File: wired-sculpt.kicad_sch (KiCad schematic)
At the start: 39 parts, among them J1 10103594-0001LF, J2 FFC3B07-30-T, J3 AVR-ISP-6 - NOT FITTED, Q1 BSS84AK,215, Q2 2N7002BK,215, SW1 FSMSM, SW2 S2B-PH-K-S(LF)(SN), U1 USBLC6-2SC6, U2 LM2776DBVT, U3 AT90USB1286-AUR, Y1 TSX-3225 16.0000MF18X-AC0

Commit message: Exclude holes and ISP from BOM
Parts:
- H1, H2, H3, J3: now left out of the parts list
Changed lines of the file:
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@@
   )
   (symbol (lib_id "Connector:AVR-ISP-6") (at 210.82 36.83 0) (mirror y) (unit 1)
-    (in_bom yes) (on_board yes)
+    (in_bom no) (on_board yes)
     (property "Reference" "J3" (id 0) (at 219.202 34.3916 0)
       (effects (font (size 1.27 1.27)) (justify right))
@@
   )
   (symbol (lib_id "Mechanical:MountingHole") (at 26.67 157.48 0) (unit 1)
-    (in_bom yes) (on_board yes)
+    (in_bom no) (on_board yes)
     (property "Reference" "H1" (id 0) (at 29.21 156.3116 0)
       (effects (font (size 1.27 1.27)) (justify left))
@@
   )
   (symbol (lib_id "Mechanical:MountingHole") (at 26.67 162.56 0) (unit 1)
-    (in_bom yes) (on_board yes)
+    (in_bom no) (on_board yes)
     (property "Reference" "H2" (id 0) (at 29.21 161.3916 0)
       (effects (font (size 1.27 1.27)) (justify left))
@@
   )
   (symbol (lib_id "Mechanical:MountingHole") (at 26.67 167.64 0) (unit 1)
-    (in_bom yes) (on_board yes)
+    (in_bom no) (on_board yes)
     (property "Reference" "H3" (id 0) (at 29.21 166.4716 0)
       (effects (font (size 1.27 1.27)) (justify left))

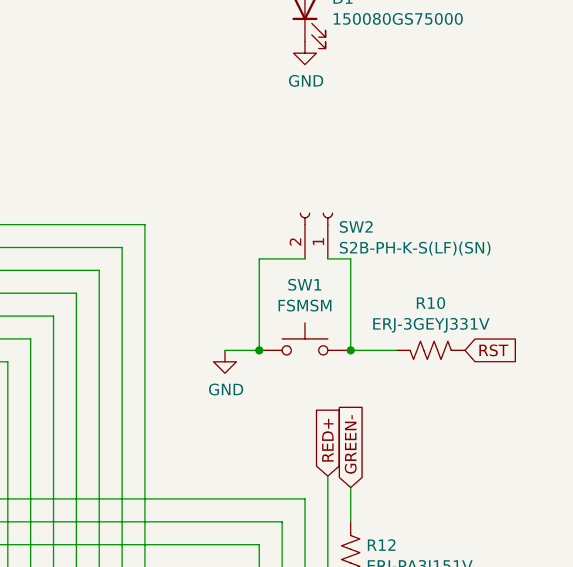
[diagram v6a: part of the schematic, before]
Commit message: Remove reset switch header
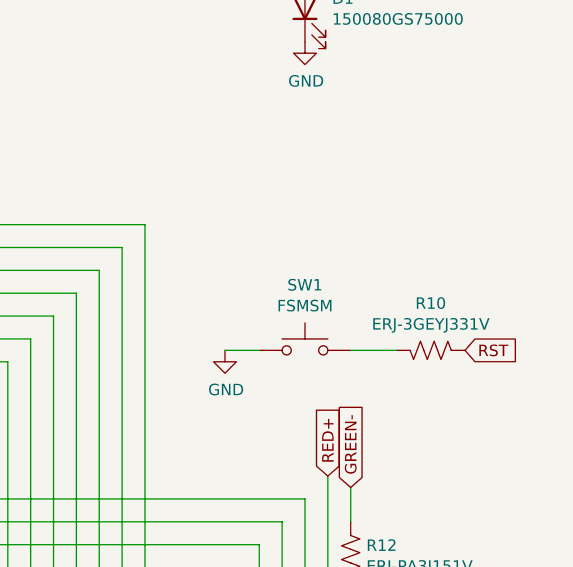
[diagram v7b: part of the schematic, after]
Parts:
- removed SW2: S2B-PH-K-S(LF)(SN), Connector_JST:JST_PH_S2B-PH-K_1x02_P2.00mm_Horizontal, symbol Connector:Conn_01x02_Female
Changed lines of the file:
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@@
   (junction (at 66.04 39.37) (diameter 0) (color 0 0 0 0)
   )
-  (junction (at 240.03 102.87) (diameter 0) (color 0 0 0 0)
-  )
   (junction (at 109.22 176.53) (diameter 0) (color 0 0 0 0)
   )
@@
   )
   (junction (at 93.98 176.53) (diameter 0) (color 0 0 0 0)
-  )
-  (junction (at 229.87 102.87) (diameter 0) (color 0 0 0 0)
   )
   (no_connect (at 43.18 73.66))
@@
     (stroke (width 0) (type default) (color 0 0 0 0))
   )
-  (wire (pts (xy 240.03 92.71) (xy 240.03 102.87))
-    (stroke (width 0) (type default) (color 0 0 0 0))
-  )
   (wire (pts (xy 191.77 55.88) (xy 156.21 55.88))
     (stroke (width 0) (type default) (color 0 0 0 0))
@@
     (stroke (width 0) (type default) (color 0 0 0 0))
   )
-  (wire (pts (xy 229.87 102.87) (xy 229.87 92.71))
-    (stroke (width 0) (type default) (color 0 0 0 0))
-  )
   (wire (pts (xy 224.79 129.54) (xy 156.21 129.54))
     (stroke (width 0) (type default) (color 0 0 0 0))
@@
     (stroke (width 0) (type default) (color 0 0 0 0))
   )
-  (wire (pts (xy 237.49 92.71) (xy 240.03 92.71))
-    (stroke (width 0) (type default) (color 0 0 0 0))
-  )
   (wire (pts (xy 66.04 29.21) (xy 71.12 29.21))
     (stroke (width 0) (type default) (color 0 0 0 0))
@@
   )
   (wire (pts (xy 107.95 46.99) (xy 100.33 46.99))
-    (stroke (width 0) (type default) (color 0 0 0 0))
-  )
-  (wire (pts (xy 229.87 92.71) (xy 234.95 92.71))
     (stroke (width 0) (type default) (color 0 0 0 0))
   )
@@
     (pin "1")
   )
-  (symbol (lib_id "Connector:Conn_01x02_Female") (at 237.49 87.63 270) (mirror x) (unit 1)
-    (in_bom yes) (on_board yes)
-    (property "Reference" "SW2" (id 0) (at 238.7092 89.2048 90)
-      (effects (font (size 1.27 1.27)) (justify left))
-    )
-    (property "Value" "S2B-PH-K-S(LF)(SN)" (id 1) (at 238.7092 91.5162 90)
-      (effects (font (size 1.27 1.27)) (justify left))
-    )
-    (property "Footprint" "Connector_JST:JST_PH_S2B-PH-K_1x02_P2.00mm_Horizontal" (id 2) (at 237.49 87.63 0)
-      (effects (font (size 1.27 1.27)) hide)
-    )
-    (property "Datasheet" "https://www.jst-mfg.com/product/pdf/eng/ePH.pdf" (id 3) (at 237.49 87.63 0)
-      (effects (font (size 1.27 1.27)) hide)
-    )
-    (property "MPN" "S2B-PH-K-S(LF)(SN)" (id 4) (at 237.49 87.63 0)
-      (effects (font (size 1.27 1.27)) hide)
-    )
-    (property "Notes" "JST connector" (id 5) (at 237.49 87.63 0)
-      (effects (font (size 1.27 1.27)) hide)
-    )
-    (pin "1")
-    (pin "2")
-  )
   (symbol (lib_id "Regulator_SwitchedCapacitor:LM2776") (at 53.34 119.38 0) (unit 1)
     (in_bom yes) (on_board yes)
@@
       (reference "SW1") (unit 1) (value "FSMSM") (footprint "Button_Switch_SMD:SW_SPST_FSMSM")
     )
-    (path "/00000000-0000-0000-0000-0000605de1fd"
-      (reference "SW2") (unit 1) (value "S2B-PH-K-S(LF)(SN)") (footprint "Connector_JST:JST_PH_S2B-PH-K_1x02_P2.00mm_Horizontal")
-    )
     (path "/00000000-0000-0000-0000-00005fcb764b"

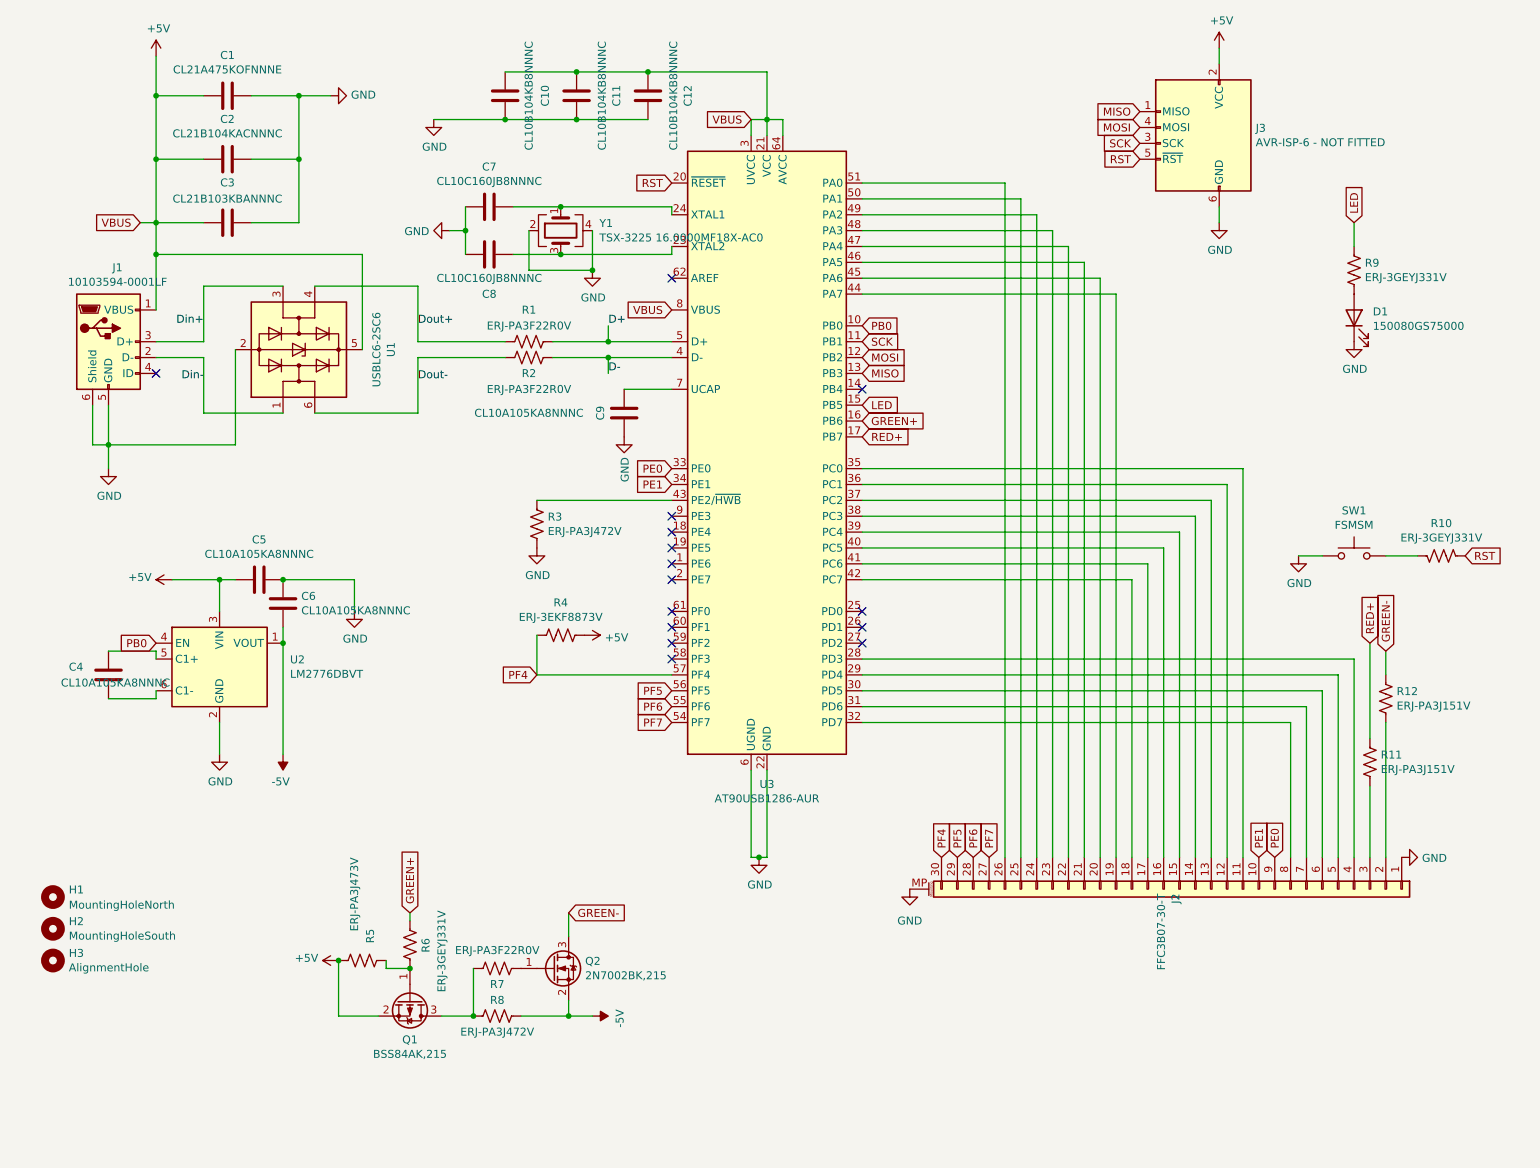
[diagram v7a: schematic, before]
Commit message: Change connector to USB-C
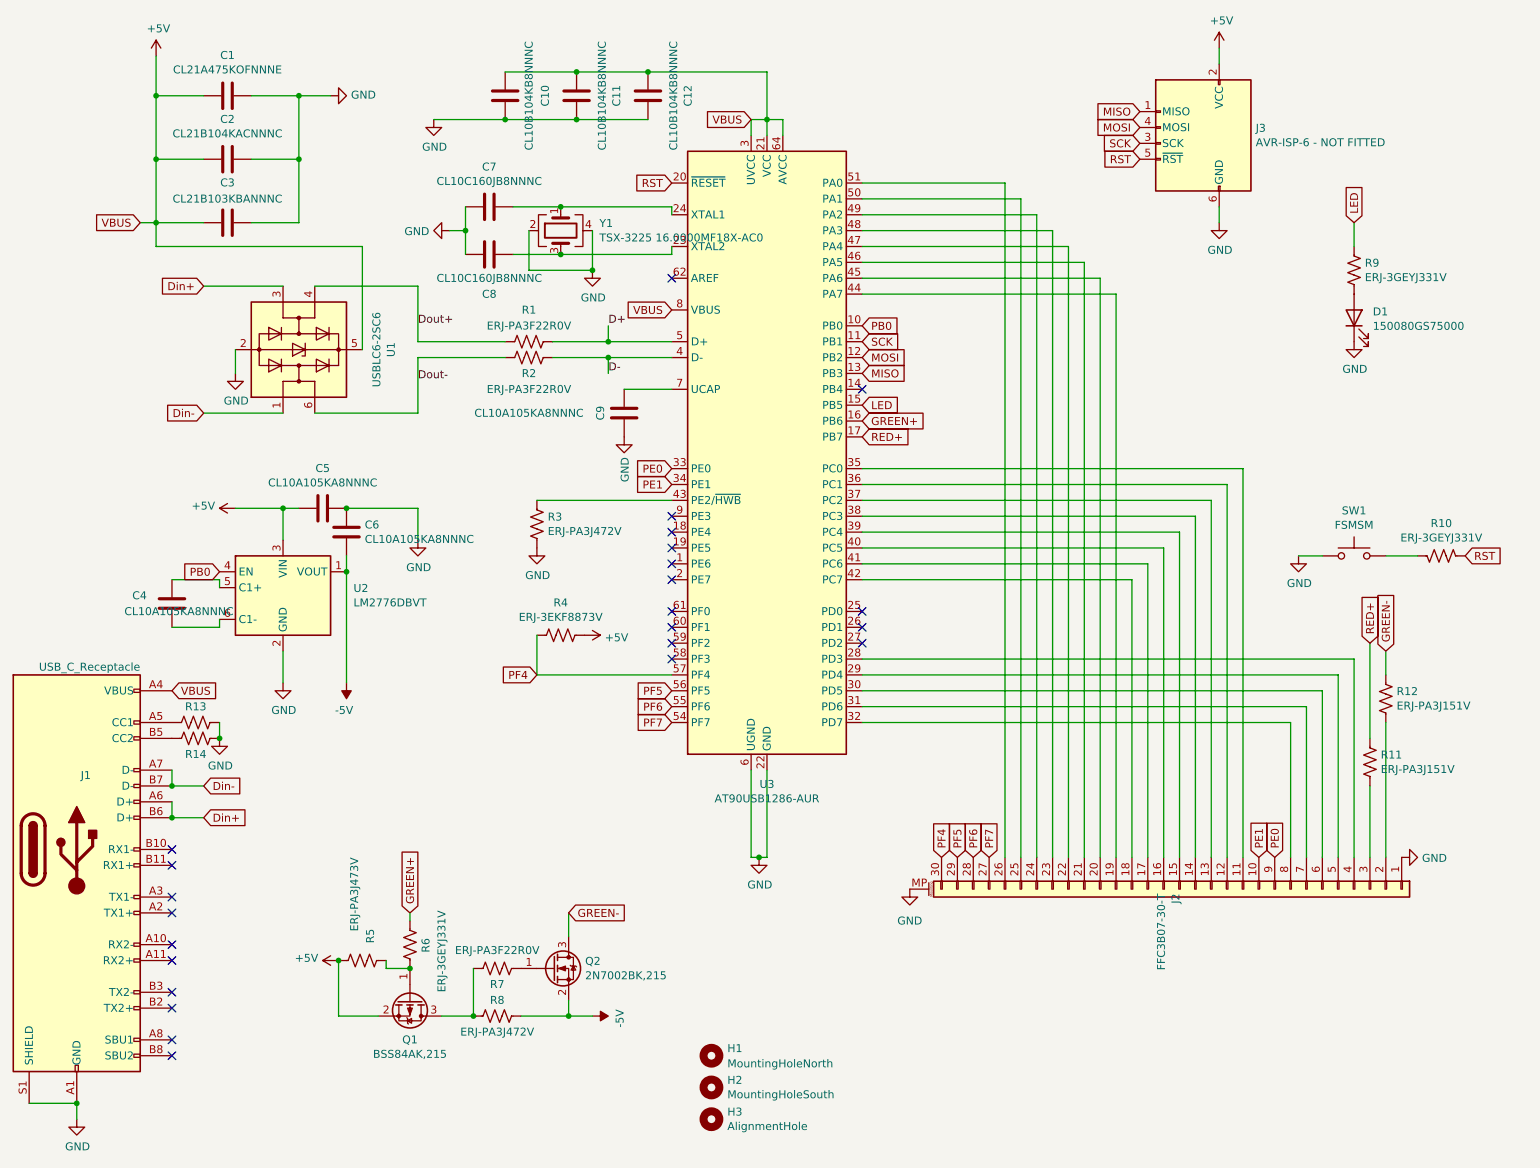
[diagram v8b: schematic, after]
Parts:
- added R13, R14: ERJ-3EKF5101V, Resistor_SMD:R_0603_1608Metric, symbol Device:R_US
- J1: value 10103594-0001LF -> USB_C_Receptacle; footprint Connector_USB:USB_Micro-B_Amphenol_10103594-0001LF_Horizontal -> Connector_USB:USB_C_Receptacle_Amphenol_12401610E4-2A; symbol Connector:USB_B_Micro -> Connector:USB_C_Receptacle; MPN 10103594-0001LF -> 12401610E4#2A; Notes USB Micro port -> USB C port
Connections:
- net +5V: now also J1.A4 (VBUS), J1.A9 (VBUS), J1.B4 (VBUS), J1.B9 (VBUS); no longer J1.1 (VBUS)
- net Din+: now also J1.A6 (D+), J1.B6 (D+); no longer J1.3 (D+)
- net Din-: now also J1.A7 (D-), J1.B7 (D-); no longer J1.2 (D-)
- net GND: now also J1.A1 (GND), J1.A12 (GND), J1.B1 (GND), J1.B12 (GND), J1.S1 (SHIELD), R13.1, R14.1; no longer J1.5 (GND), J1.6 (Shield)
- new net: J1.A5 (CC1), R13.2
- new net: J1.B5 (CC2), R14.2
- no-connect marks 15 -> 24
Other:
- moved on the sheet: C4, C5, C6, H1, H2, H3, U2
